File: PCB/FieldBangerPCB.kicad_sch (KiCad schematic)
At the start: 11 parts, among them J1 8P8C, SW1 SW_SPST, SW2 SW_SPST, SW3 SW_SPST, SW4 SW_SPST, SW5 SW_SPST, SW6 SW_SPST, SW7 SW_SPST, SW8 SW_SPST, SW9 SW_SPST

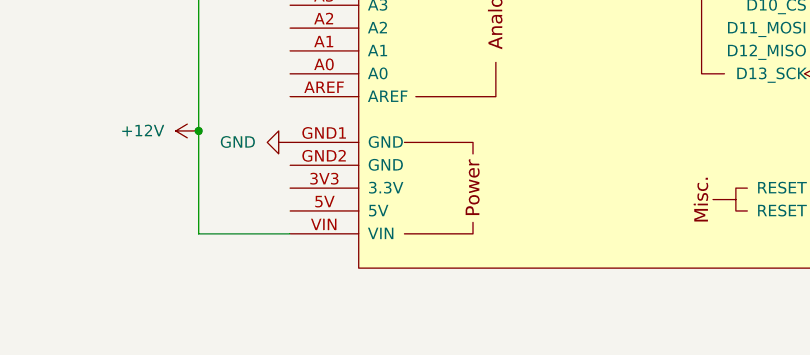
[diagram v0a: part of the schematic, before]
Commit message: added power cap
added 180uF cap to power input to help with power filtering.
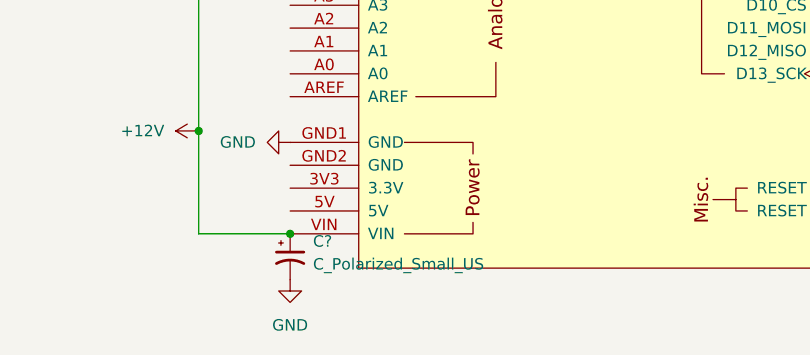
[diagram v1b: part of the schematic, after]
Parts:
- added C?: C_Polarized_Small_US, symbol Device:C_Polarized_Small_US
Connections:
- net +12V: now also C?.1
- net GND: now also C?.2
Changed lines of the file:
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@@
   (junction (at 55.88 82.55) (diameter 0) (color 0 0 0 0)
+  )
+  (junction (at 85.09 111.76) (diameter 0) (color 0 0 0 0)
   )
   (wire (pts (xy 85.09 68.58) (xy 71.12 68.58))
@@
     (pin "VIN")
   )
+  (symbol (lib_id "power:GND") (at 85.09 116.84 0) (unit 1)
+    (in_bom yes) (on_board yes) (fields_autoplaced)
+    (property "Reference" "#PWR?" (id 0) (at 85.09 123.19 0)
+      (effects (font (size 1.27 1.27)) hide)
+    )
+    (property "Value" "GND" (id 1) (at 85.09 121.92 0))
+    (property "Footprint" "" (id 2) (at 85.09 116.84 0)
+      (effects (font (size 1.27 1.27)) hide)
+    )
+    (property "Datasheet" "" (id 3) (at 85.09 116.84 0)
+      (effects (font (size 1.27 1.27)) hide)
+    )
+    (pin "1")
+  )
   (symbol (lib_id "Switch:SW_SPST") (at 156.21 86.36 0) (unit 1)
     (in_bom yes) (on_board yes) (fields_autoplaced)
@@
     )
     (property "Datasheet" "~" (id 3) (at 171.45 73.66 0)
+      (effects (font (size 1.27 1.27)) hide)
+    )
+    (pin "1")
+    (pin "2")
+  )
+  (symbol (lib_id "Device:C_Polarized_Small_US") (at 85.09 114.3 0) (unit 1)
+    (in_bom yes) (on_board yes) (fields_autoplaced)
+    (property "Reference" "C?" (id 0) (at 87.63 112.5981 0)
+      (effects (font (size 1.27 1.27)) (justify left))
+    )
+    (property "Value" "C_Polarized_Small_US" (id 1) (at 87.63 115.1381 0)
+      (effects (font (size 1.27 1.27)) (justify left))
+    )
+    (property "Footprint" "" (id 2) (at 85.09 114.3 0)
+      (effects (font (size 1.27 1.27)) hide)
+    )
+    (property "Datasheet" "~" (id 3) (at 85.09 114.3 0)
       (effects (font (size 1.27 1.27)) hide)
     )
@@
       (reference "#PWR0104") (unit 1) (value "+12V") (footprint "")
     )
+    (path "/2827b060-e8b6-429e-98cb-12300f5f9a2d"
+      (reference "#PWR?") (unit 1) (value "GND") (footprint "")
+    )
+    (path "/87e9ff73-5090-4100-8836-0ddbce8895fa"
+      (reference "C?") (unit 1) (value "C_Polarized_Small_US") (footprint "")
+    )
     (path "/ffcee465-3d20-4d5b-84bd-996b060505a2"
